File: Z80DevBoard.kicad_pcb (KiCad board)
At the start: 2 copper layers, 219 x 107.5 mm, 145 parts, among them SW1 WAIT, SW2 RESET, SW3 Z80BOOT, SW4 RPBOOT

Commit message: Added 2 layers.
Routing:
- added copper zone on In2.Cu, net GND
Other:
- copper layers 2 -> 4
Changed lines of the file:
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@@
 	(layers
 		(0 "F.Cu" signal)
+		(4 "In1.Cu" signal)
+		(6 "In2.Cu" signal)
 		(2 "B.Cu" signal)
 		(9 "F.Adhes" user "F.Adhesive")
@@
 	)
 	(setup
+		(stackup
+			(layer "F.SilkS"
+				(type "Top Silk Screen")
+			)
+			(layer "F.Paste"
+				(type "Top Solder Paste")
+			)
+			(layer "F.Mask"
+				(type "Top Solder Mask")
+				(thickness 0.01)
+			)
+			(layer "F.Cu"
+				(type "copper")
+				(thickness 0.035)
+			)
+			(layer "dielectric 1"
+				(type "prepreg")
+				(thickness 0.1)
+				(material "FR4")
+				(epsilon_r 4.5)
+				(loss_tangent 0.02)
+			)
+			(layer "In1.Cu"
+				(type "copper")
+				(thickness 0.035)
+			)
+			(layer "dielectric 2"
+				(type "core")
+				(thickness 1.24)
+				(material "FR4")
+				(epsilon_r 4.5)
+				(loss_tangent 0.02)
+			)
+			(layer "In2.Cu"
+				(type "copper")
+				(thickness 0.035)
+			)
+			(layer "dielectric 3"
+				(type "prepreg")
+				(thickness 0.1)
+				(material "FR4")
+				(epsilon_r 4.5)
+				(loss_tangent 0.02)
+			)
+			(layer "B.Cu"
+				(type "copper")
+				(thickness 0.035)
+			)
+			(layer "B.Mask"
+				(type "Bottom Solder Mask")
+				(thickness 0.01)
+			)
+			(layer "B.Paste"
+				(type "Bottom Solder Paste")
+			)
+			(layer "B.SilkS"
+				(type "Bottom Silk Screen")
+			)
+			(copper_finish "None")
+			(dielectric_constraints no)
+		)
 		(pad_to_mask_clearance 0)
 		(allow_soldermask_bridges_in_footprints no)
@@
 		(net 214)
 	)
+	(zone
+		(net 20)
+		(net_name "GND")
+		(layer "In2.Cu")
+		(hatch edge 0.5)
+		(connect_pads
+			(clearance 0.5)
+		)
+		(min_thickness 0.25)
+		(filled_areas_thickness no)
+		(fill yes
+			(thermal_gap 0.5)
+			(thermal_bridge_width 0.5)
+		)
+		(polygon
+			(pts
+				(xy 257 146) (xy 38 146) (xy 38 38.5) (xy 257 38.5)
+			)
+		)
+	)
 	(embedded_fonts no)

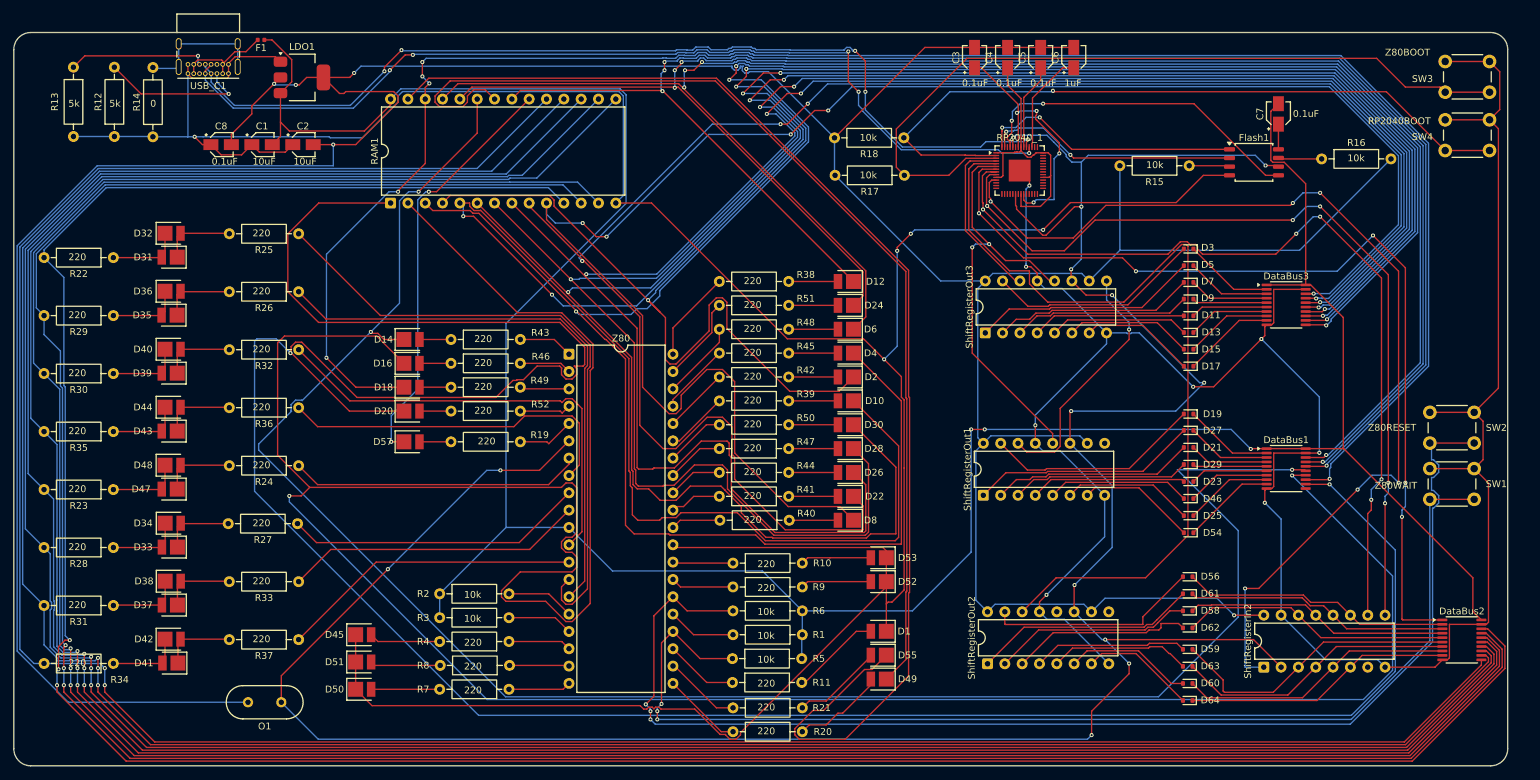
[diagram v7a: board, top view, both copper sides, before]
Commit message: Added the vcc and 3v3 layer. Fixed the GND layer.
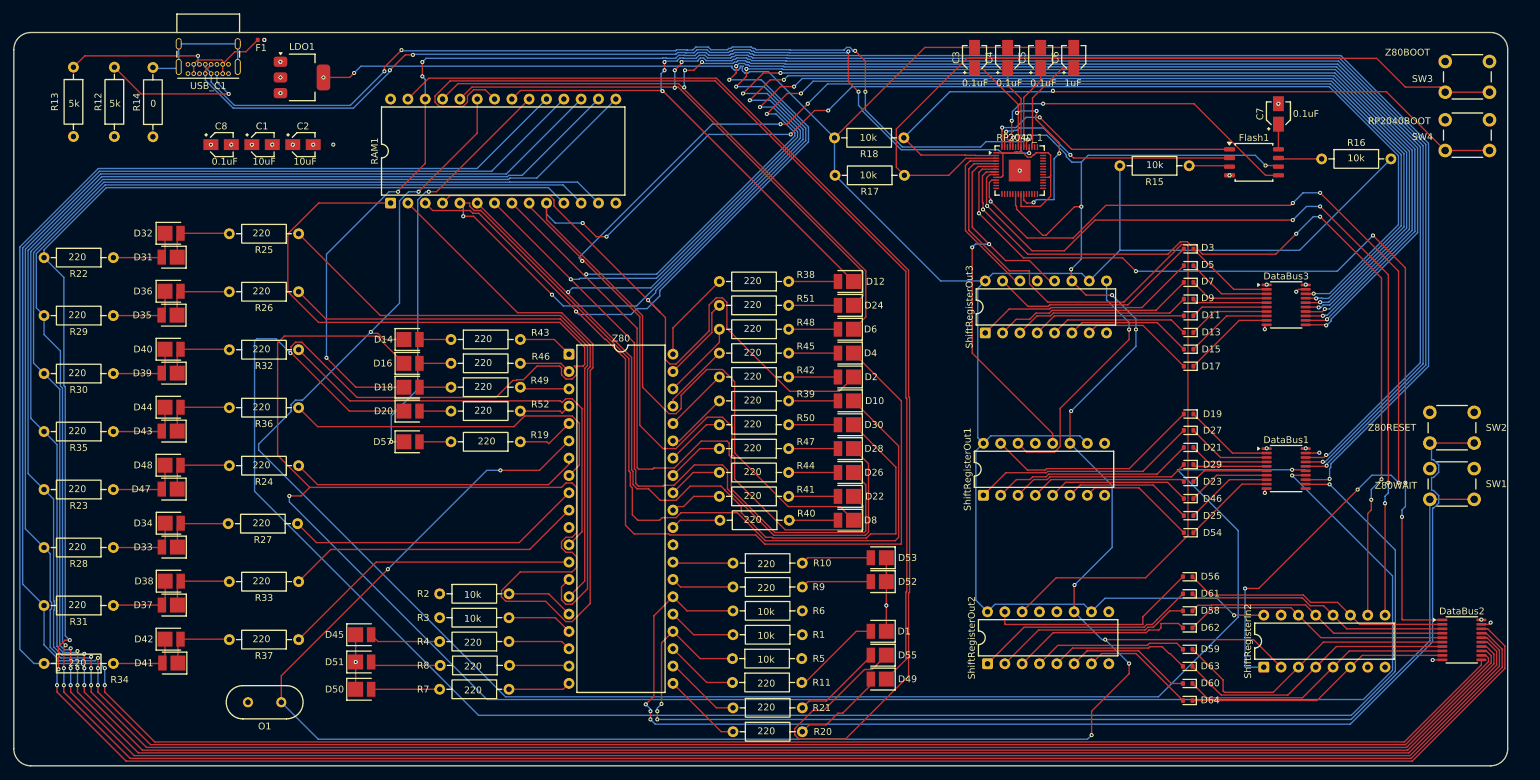
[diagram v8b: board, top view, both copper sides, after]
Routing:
- net GND: track 792.6 -> 32.5 mm, vias 13 -> 14
- net Vdd_3v3: track 545.6 -> 378.7 mm, vias 5 -> 7
- net Vcc: track 415.7 -> 382.4 mm, vias 3 -> 9
- net CLOCK: track 391.2 -> 373.5 mm
- net RAM-A13: track 276.7 -> 276.2 mm, vias 6 -> 5
